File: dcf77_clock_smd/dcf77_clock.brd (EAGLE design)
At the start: 83.1 x 76.2 mm, 42 parts, among them IC1 7805DT, IC2 ATMEGA48/88/168-AU, J2 DCJ0202, Q1 32.768kHz, Q2 IRLML6244TRPBF, SW1 EC12E_SW, U1 LCD-16X2SILK, U2 DS1307SO8

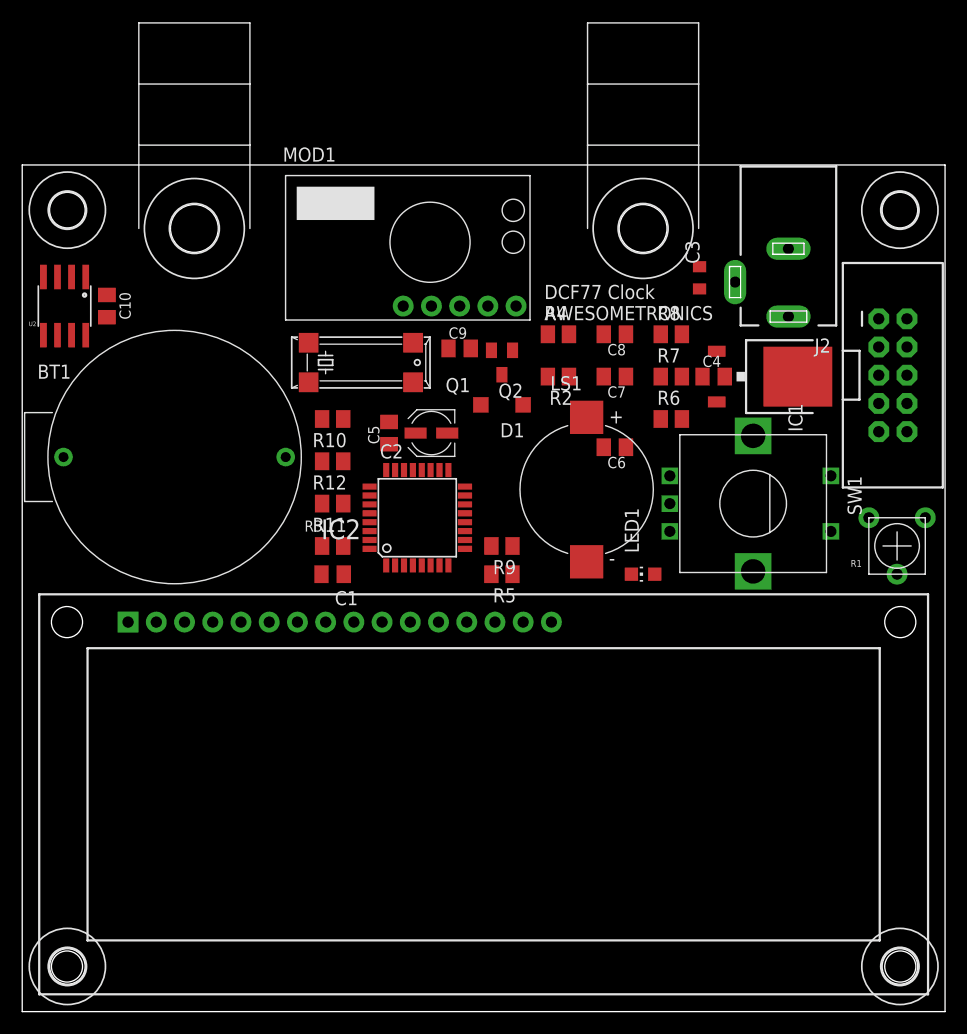
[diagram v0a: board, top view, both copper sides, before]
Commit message: Replace incorrect footprints
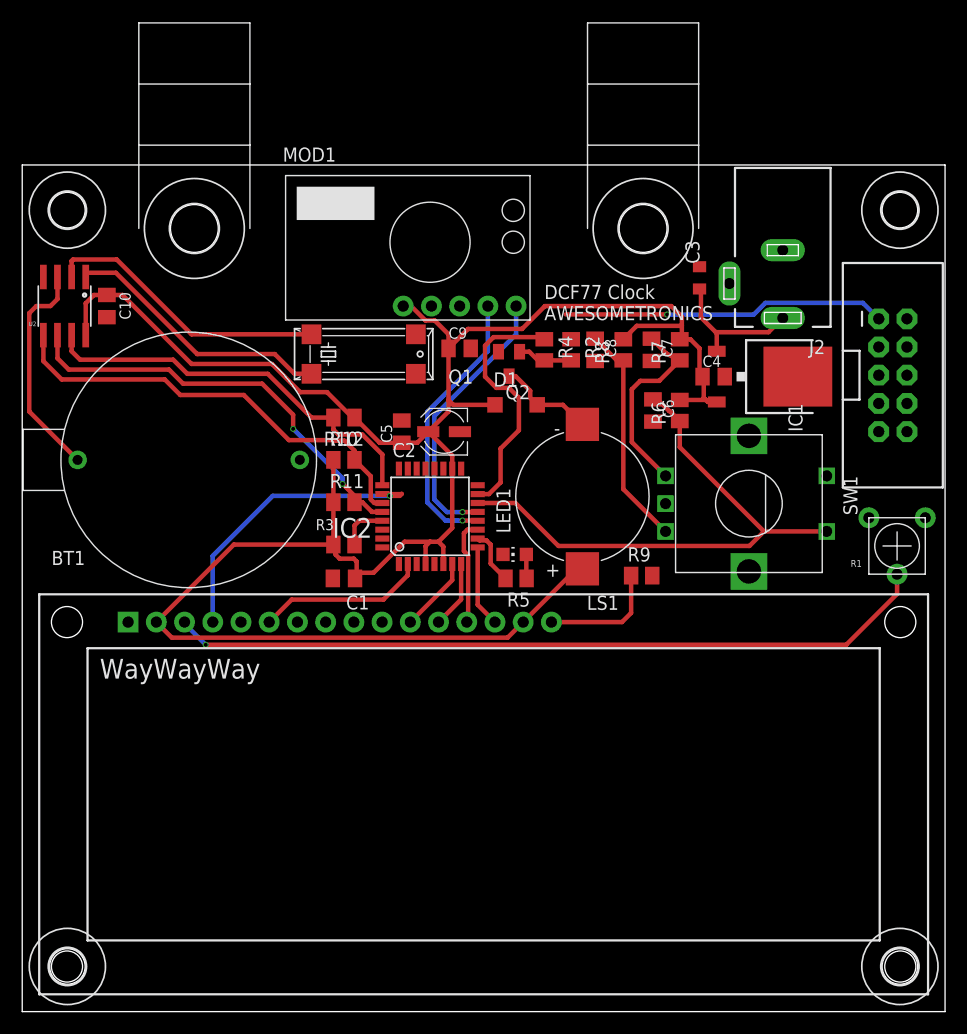
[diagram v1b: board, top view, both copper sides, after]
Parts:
- BT1: value CONNFLYDS1092-04-B6P -> CR2032_HOLDER14; device _mlokc:CONNFLYDS1092-04-B6P -> dcf77:CONNFLY-DS1092-14-B6P
- moved R9 12.9 mm to (55.8, 39.2), turned to 0 degrees
- moved LED1 11.7 mm to (44.3, 41.1)
- moved C6 4.76 mm to (56.8, 54.1), turned to 270 degrees
- moved R8 4.54 mm to (54.1, 59.6), turned to 90 degrees
- moved C7 4.09 mm to (56.6, 59.6), turned to 270 degrees
- moved R2 2.67 mm to (49.4, 59.6), turned to 270 degrees
- moved R7 2.53 mm to (59.2, 59.6), turned to 90 degrees
- moved C8 2.26 mm to (51.6, 59.6), turned to 270 degrees
- moved R4 1.89 mm to (47.0, 59.6), turned to 270 degrees
- moved R5 1.33 mm to (44.5, 39.0)
- moved BT1 1.30 mm to (15.0, 49.7)
- moved D1 1.27 mm to (44.5, 54.6), turned to 0 degrees
- moved C2 1.15 mm to (38.0, 52.2)
- moved IC2 1.15 mm to (36.7, 44.6)
- moved C5 1.15 mm to (34.2, 52.2)
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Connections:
- net GND: now also BT1.MINUS; no longer BT1.P$1
- net LCD_RS: now also IC2.26; no longer IC2.25
- net N$12: now also BT1.PLUS; no longer BT1.P$2
- net RTC_SQW: now also IC2.25; no longer IC2.26
- net SW: now also IC2.14; no longer IC2.19
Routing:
- net VCC: track 0.00 -> 197.1 mm
- net N$7: track 0.00 -> 68.7 mm, vias 0 -> 1
- net ISP_MOSI_BUZ_PWM: track 0.00 -> 52.5 mm, vias 0 -> 1
- net SW: track 0.00 -> 49.8 mm
- net RTC_SDA: track 0.00 -> 39.8 mm
- net RTC_SCL: track 0.00 -> 38.4 mm, vias 0 -> 2
- net RTC_SQW: track 0.00 -> 36.7 mm
- net LCD_RS: track 0.00 -> 27.0 mm, vias 0 -> 1
- net N$11: track 0.00 -> 25.9 mm
- net DCF77_OUT: track 0.00 -> 25.2 mm, vias 0 -> 1
- net DCF77_SEL: track 0.00 -> 24.9 mm, vias 0 -> 1
- net N$10: track 0.00 -> 24.5 mm
- net ENC_B: track 0.00 -> 20.3 mm
- net N$12: track 0.00 -> 20.1 mm
- net ENC_A: track 0.00 -> 17.8 mm
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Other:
- board text added: "WayWayWay"

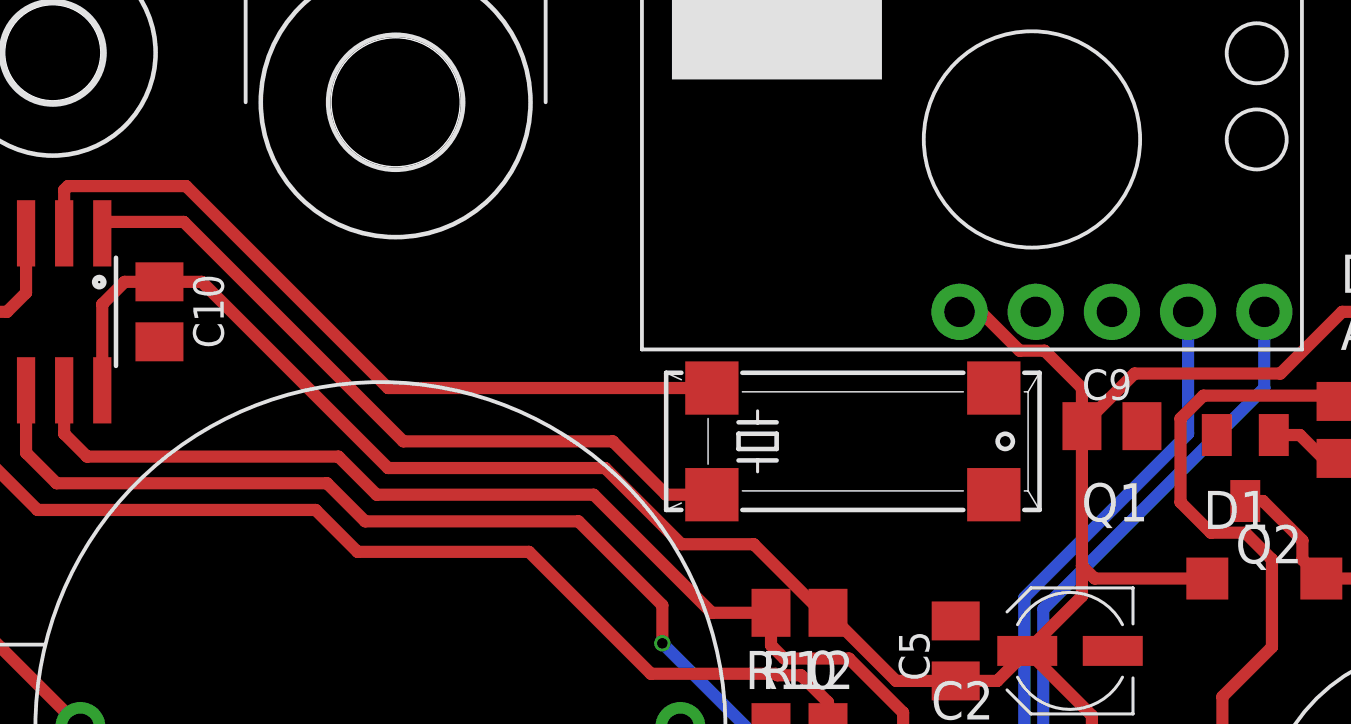
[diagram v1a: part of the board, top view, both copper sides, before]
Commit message: Change oscillator footprint
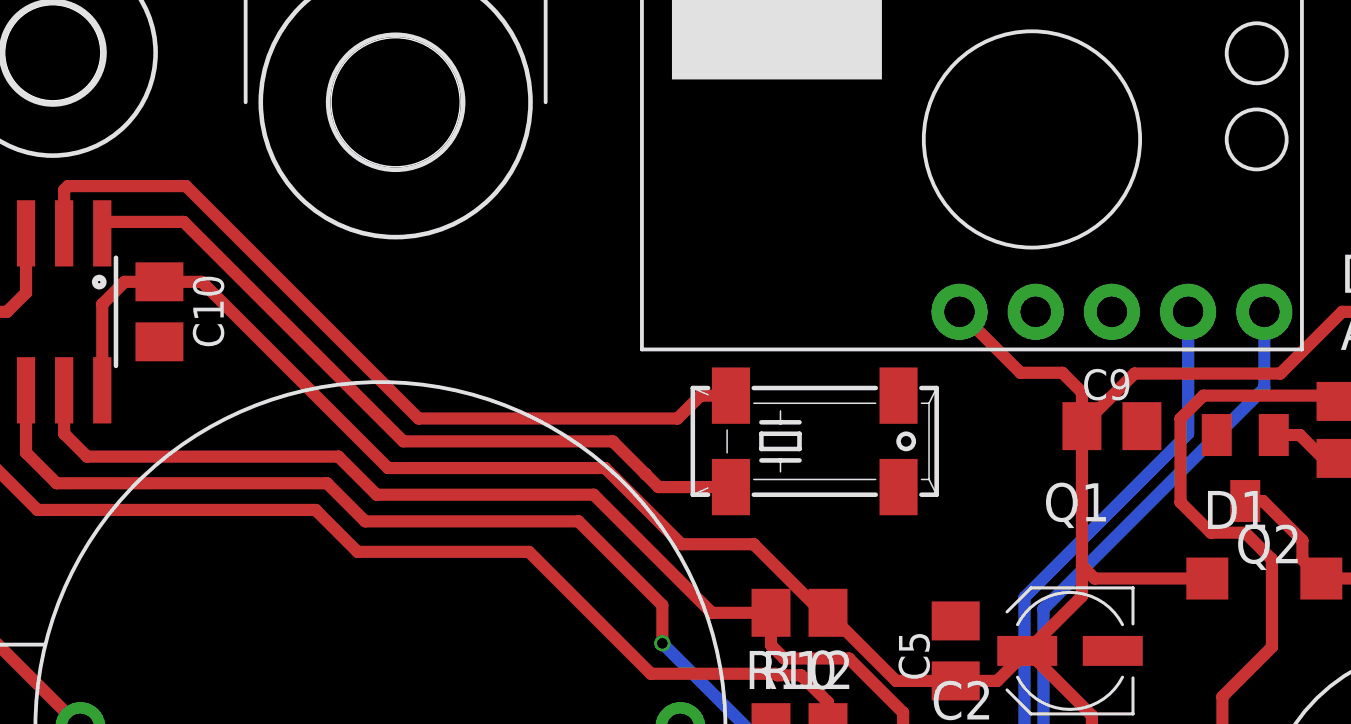
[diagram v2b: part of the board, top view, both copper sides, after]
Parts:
- Q1: device crystal:MM39SL -> crystal:MM20SS
- moved Q1 1.27 mm to (29.5, 59.2)
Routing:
- net N$11: track 25.9 -> 27.2 mm
- net N$10: track 24.5 -> 25.0 mm
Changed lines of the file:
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@@
 <attribute name="NAME" x="23.45" y="76.5" size="1.27" layer="25"/>
 </element>
-<element name="Q1" library="crystal" library_urn="urn:adsk.eagle:library:204" package="MM39SL" package3d_urn="urn:adsk.eagle:package:12090/1" value="32.768kHz" x="30.734" y="59.182" smashed="yes">
-<attribute name="MF" value="" x="30.734" y="59.182" size="1.778" layer="27" display="off"/>
-<attribute name="MPN" value="" x="30.734" y="59.182" size="1.778" layer="27" display="off"/>
-<attribute name="NAME" x="38.354" y="56.515" size="1.27" layer="25" ratio="10"/>
-<attribute name="OC_FARNELL" value="unknown" x="30.734" y="59.182" size="1.778" layer="27" display="off"/>
-<attribute name="OC_NEWARK" value="unknown" x="30.734" y="59.182" size="1.778" layer="27" display="off"/>
-<attribute name="POPULARITY" value="0" x="98.044" y="-50.038" size="1.778" layer="27" display="off"/>
-<attribute name="VALUE" x="25.654" y="55.245" size="1.27" layer="27" ratio="10"/>
+<element name="Q1" library="crystal" library_urn="urn:adsk.eagle:library:204" package="MM20SS" package3d_urn="urn:adsk.eagle:package:12092/1" value="32.768kHz" x="29.464" y="59.182" smashed="yes">
+<attribute name="MF" value="" x="29.464" y="59.182" size="1.778" layer="27" display="off"/>
+<attribute name="MPN" value="" x="29.464" y="59.182" size="1.778" layer="27" display="off"/>
+<attribute name="NAME" x="37.084" y="56.515" size="1.27" layer="25" ratio="10"/>
+<attribute name="OC_FARNELL" value="unknown" x="29.464" y="59.182" size="1.778" layer="27" display="off"/>
+<attribute name="OC_NEWARK" value="unknown" x="29.464" y="59.182" size="1.778" layer="27" display="off"/>
+<attribute name="POPULARITY" value="4" x="96.774" y="-50.038" size="1.778" layer="27" display="off"/>
+<attribute name="VALUE" x="24.384" y="55.245" size="1.27" layer="27" ratio="10"/>
 </element>
 <element name="R1" library="SparkFun" package="TRIM_POT_PTH" value="10k" x="78.74" y="41.91" smashed="yes" rot="R180">
@@
 <wire x1="38.37" y1="54.019" x2="38.37" y2="55.035" width="0.4064" layer="1"/>
 <wire x1="38.37" y1="55.035" x2="38.37" y2="59.69" width="0.4064" layer="1"/>
-<wire x1="38.37" y1="60.96" x2="38.37" y2="59.69" width="0.4064" layer="1"/>
 <wire x1="28.006" y1="42.037" x2="28.006" y2="45.847" width="0.4064" layer="1"/>
 <wire x1="29.956" y1="38.989" x2="30.099" y2="38.989" width="0.4064" layer="1"/>
@@
 <wire x1="59.182" y1="55.052" x2="61.402" y2="55.052" width="0.4064" layer="1"/>
 <wire x1="61.402" y1="55.052" x2="61.468" y2="55.118" width="0.4064" layer="1"/>
-<wire x1="36.293425" y1="62.2046" x2="37.1254" y2="62.2046" width="0.4064" layer="1"/>
-<wire x1="37.1254" y1="62.2046" x2="38.37" y2="60.96" width="0.4064" layer="1"/>
-<wire x1="34.29" y1="63.5" x2="34.998025" y2="63.5" width="0.4064" layer="1"/>
-<wire x1="34.998025" y1="63.5" x2="36.293425" y2="62.2046" width="0.4064" layer="1"/>
+<wire x1="34.29" y1="63.5" x2="36.322" y2="61.468" width="0.4064" layer="1"/>
+<wire x1="36.322" y1="61.468" x2="37.719" y2="61.468" width="0.4064" layer="1"/>
+<wire x1="37.719" y1="61.468" x2="38.37" y2="60.817" width="0.4064" layer="1"/>
+<wire x1="38.37" y1="60.817" x2="38.37" y2="59.69" width="0.4064" layer="1"/>
 <wire x1="81.28" y1="44.45" x2="79.629" y2="62.357" width="0" layer="19" extent="1-1"/>
 <wire x1="62.51" y1="54.87" x2="79.629" y2="62.357" width="0" layer="19" extent="1-1"/>
@@
 <wire x1="5.715" y1="66.1162" x2="5.715" y2="66.4972" width="0.4064" layer="1"/>
 <wire x1="22.733" y1="59.182" x2="15.748" y2="59.182" width="0.4064" layer="1"/>
-<wire x1="24.511" y1="57.404" x2="26.035" y2="57.404" width="0.4064" layer="1"/>
-<wire x1="24.511" y1="57.404" x2="22.733" y2="59.182" width="0.4064" layer="1"/>
+<wire x1="23.832203125" y1="58.082796875" x2="23.8125" y2="58.1025" width="0.4064" layer="1"/>
+<wire x1="23.8125" y1="58.1025" x2="22.733" y2="59.182" width="0.4064" layer="1"/>
 <wire x1="8.4328" y1="66.4972" x2="15.748" y2="59.182" width="0.4064" layer="1"/>
+<wire x1="23.832203125" y1="58.082796875" x2="24.257" y2="57.658" width="0.4064" layer="1"/>
+<wire x1="24.257" y1="57.658" x2="26.67" y2="57.658" width="0.4064" layer="1"/>
 </signal>
 <signal name="N$11">
@@
 <contactref element="Q1" pad="4"/>
 <wire x1="4.445" y1="66.1162" x2="4.445" y2="67.564" width="0.4064" layer="1"/>
-<wire x1="15.24" y1="60.96" x2="26.035" y2="60.96" width="0.4064" layer="1"/>
 <wire x1="4.445" y1="67.564" x2="4.572" y2="67.691" width="0.4064" layer="1"/>
 <wire x1="4.572" y1="67.691" x2="8.509" y2="67.691" width="0.4064" layer="1"/>
-<wire x1="8.509" y1="67.691" x2="15.24" y2="60.96" width="0.4064" layer="1"/>
+<wire x1="16.256" y1="59.944" x2="24.892" y2="59.944" width="0.4064" layer="1"/>
+<wire x1="25.654" y1="60.706" x2="26.67" y2="60.706" width="0.4064" layer="1"/>
+<wire x1="8.509" y1="67.691" x2="16.256" y2="59.944" width="0.4064" layer="1"/>
+<wire x1="24.892" y1="59.944" x2="25.654" y2="60.706" width="0.4064" layer="1"/>
 </signal>
 <signal name="N$12">

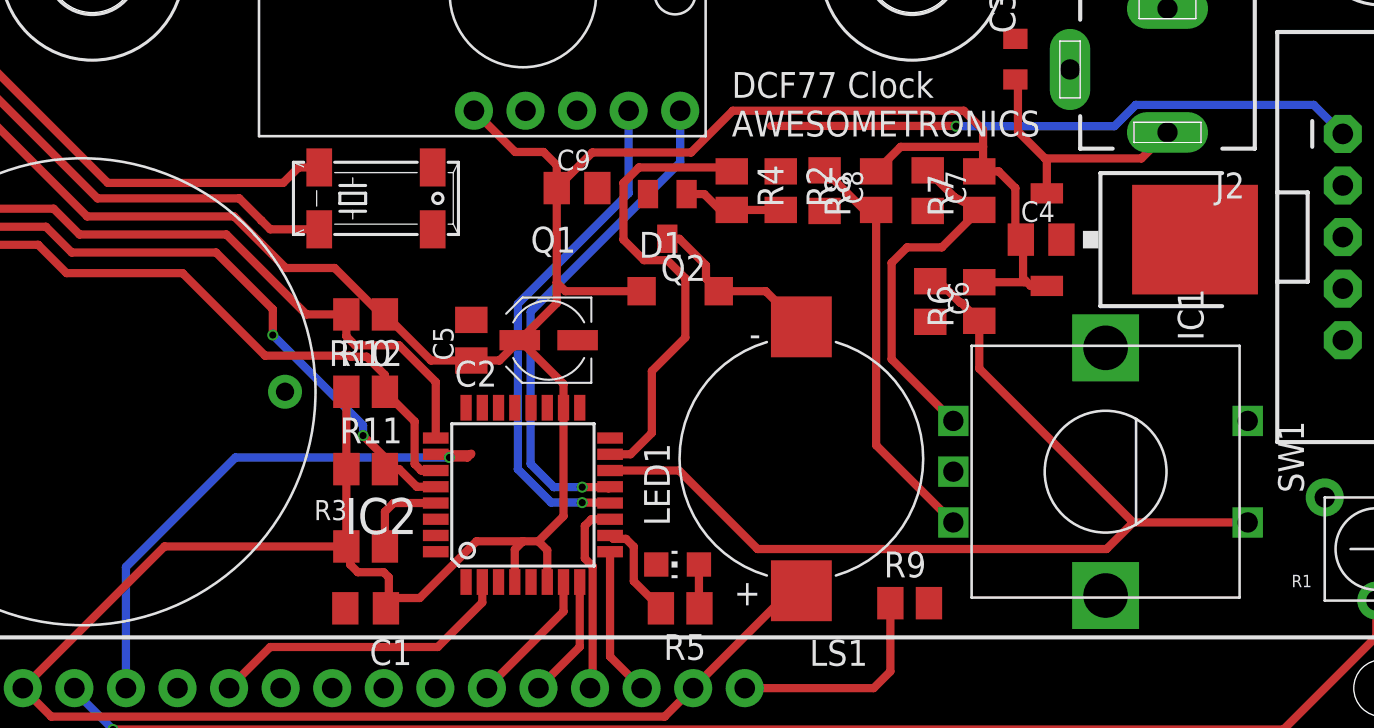
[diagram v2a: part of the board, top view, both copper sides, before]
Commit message: Add encoder connections
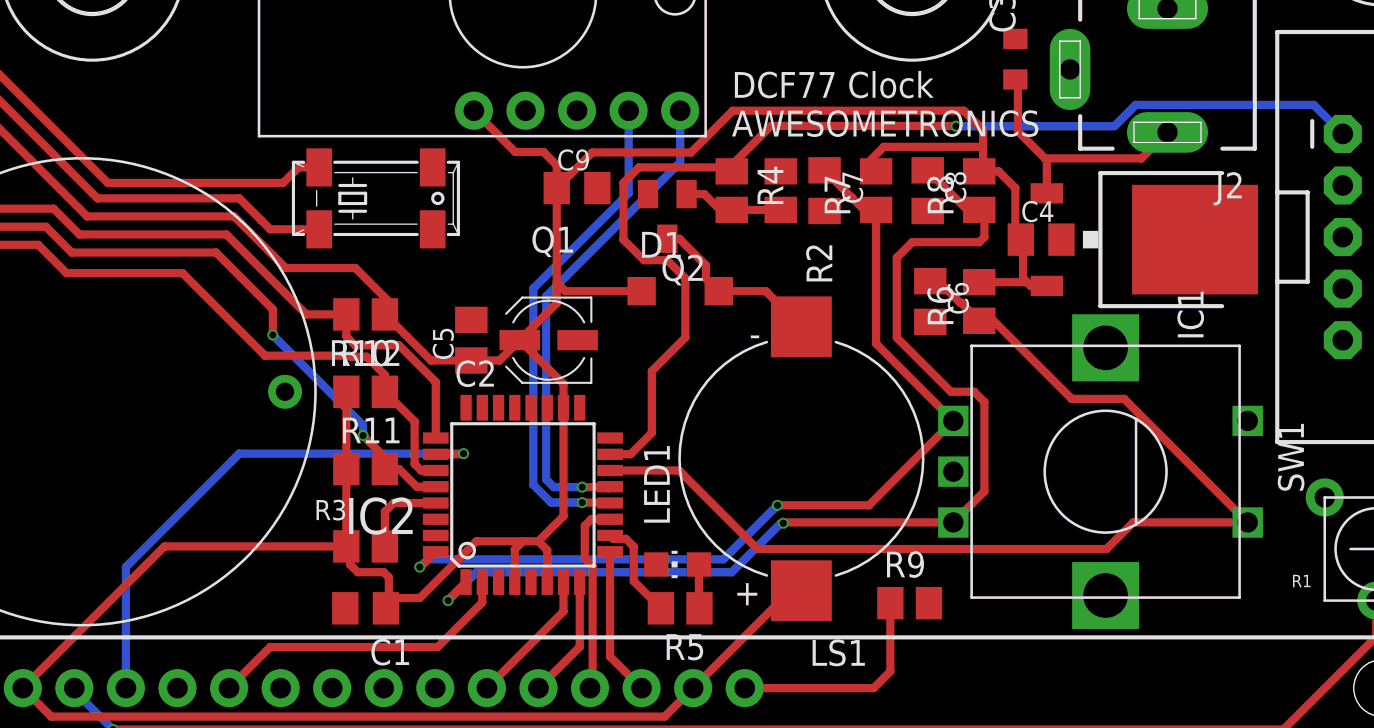
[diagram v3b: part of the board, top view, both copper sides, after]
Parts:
- moved C7 5.08 mm to (51.6, 59.6)
- moved C8 5.08 mm to (56.6, 59.6)
- moved R7 5.08 mm to (54.1, 59.6)
- moved R8 5.08 mm to (59.2, 59.6)
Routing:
- net ENC_B: track 20.3 -> 53.4 mm, vias 0 -> 2
- net ENC_A: track 17.8 -> 45.8 mm, vias 0 -> 2
- net SW: track 49.8 -> 54.1 mm
- net ISP_MOSI_BUZ_PWM: track 52.5 -> 55.6 mm
- net VCC: track 197.0 -> 198.3 mm
- net LCD_RS: track 27.0 -> 26.3 mm
- net DCF77_OUT: track 25.2 -> 24.5 mm
- net DCF77_SEL: track 24.9 -> 24.3 mm
